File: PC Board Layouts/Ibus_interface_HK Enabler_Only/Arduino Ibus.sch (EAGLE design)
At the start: 14 parts

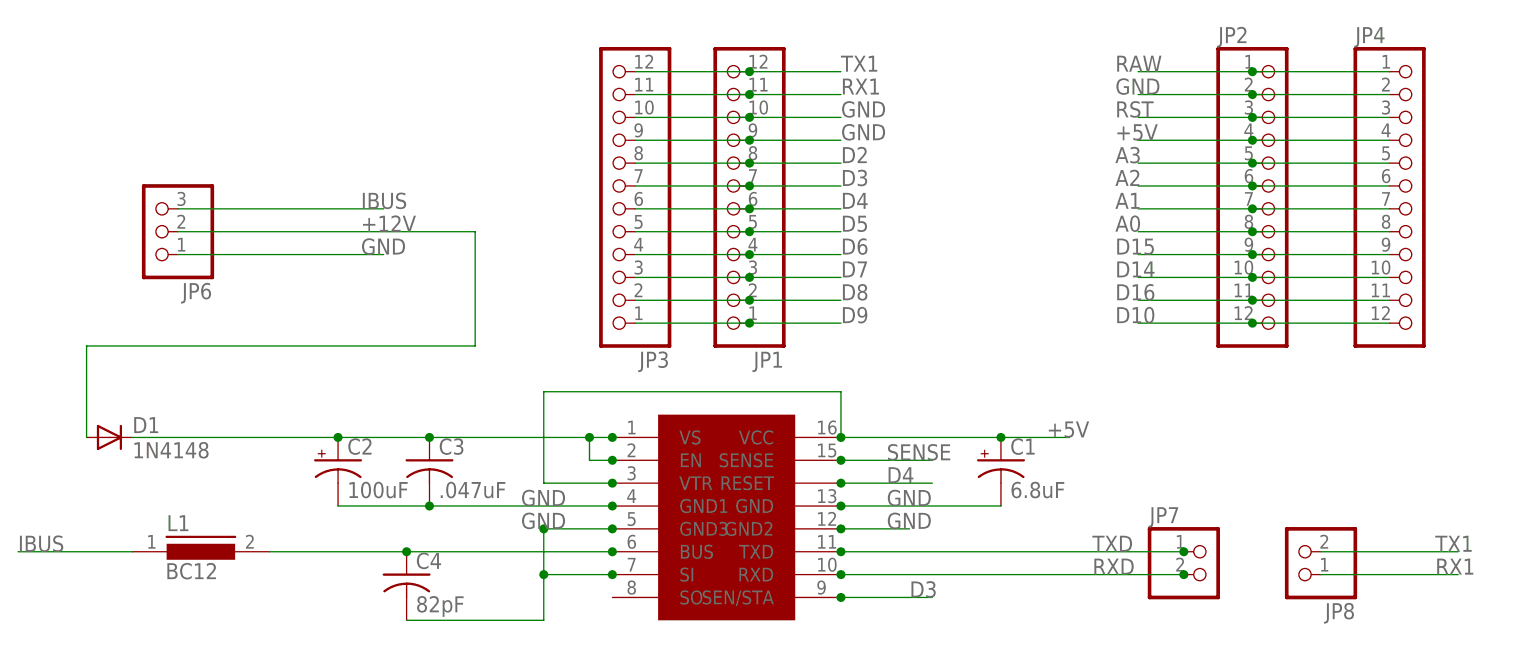
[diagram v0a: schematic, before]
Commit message: Changed Brute Force PCB to be smaller with no options
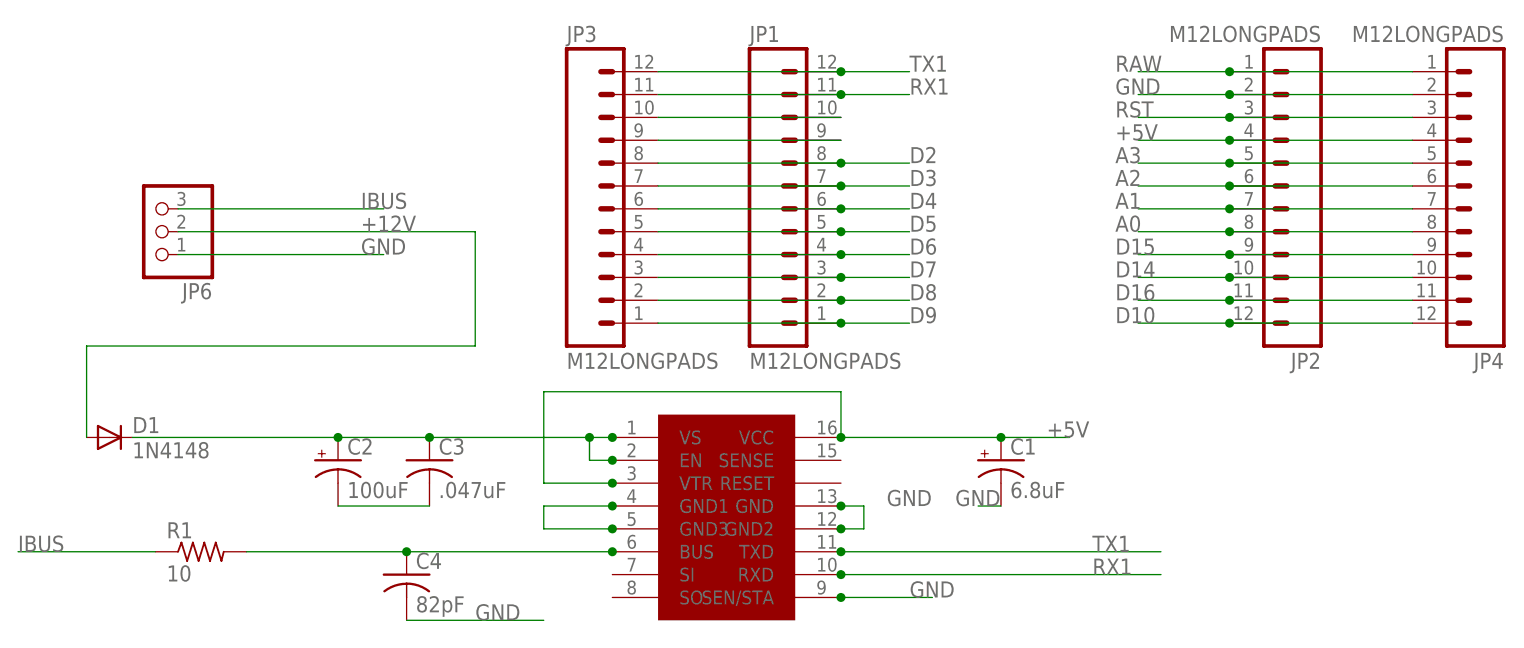
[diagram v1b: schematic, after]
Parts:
- removed JP7, JP8: (no value), pinhead:PINHD-1X2
- removed L1: BC12, inductors:BC12
- added R1: 10, resistor:R-US_0207/7
- JP1, JP2, JP3, JP4: value (none) -> M12LONGPADS; device pinhead:PINHD-1X12 -> SparkFun-Connectors:M12LONGPADS
- JP6: device pinhead:PINHD-1X3/90 -> pinhead:PINHD-1X3
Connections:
- removed net RXD: JP7.2, U$1.RXD
- removed net SENSE: U$1.SENSE
- removed net TXD: JP7.1, U$1.TXD
- new net N$1: JP1.10, JP3.10
- new net N$2: JP1.9, JP3.9
- net D3: no longer U$1.SEN/STA
- net D4: no longer U$1.RESET
- net GND: now also U$1.SEN/STA; no longer JP1.10, JP1.9, JP3.10, JP3.9, U$1.SI
- net IBUS: now also R1.1; no longer L1.1
- net N$4: now also R1.2; no longer L1.2
- net RX1: now also U$1.RXD; no longer JP8.1
- net TX1: now also U$1.TXD; no longer JP8.2
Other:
- moved on the sheet: JP1, JP2, JP3, JP4
